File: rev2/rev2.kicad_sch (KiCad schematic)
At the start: 118 parts, among them J1 USB_C_Receptacle_USB2.0_14P, Q1 BSS138, Q10 BSS138, Q11 BSS138, Q12 BSS138, Q13 BSS138, Q14 BSS138, Q15 BSS138, Q16 BSS138, Q2 BSS138, Q3 BSS138, Q4 BSS138, Q5 BSS138, Q6 BSS138, Q7 BSS138, Q8 BSS138, Q9 BSS138, SW1 SW_Push, SW2 SW_Push, SW3 SW_Push, SW4 SW_Push, SW5 SW_Push, SW6 SW_Push, SW7 SW_Push, SW8 SW_Push, U1 CH340N, U2 ATtiny1604-SS, U3 74HC595, U4 74HC595, U5 74HC595, U6 74HC595

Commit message: aw がんばった
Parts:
- renumbered C3 to C2, C2 to C3
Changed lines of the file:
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@@
 		(dnp no)
 		(fields_autoplaced yes)
-		(property "Reference" "C3"
+		(property "Reference" "C2"
 			(at 41.91 220.9799 0)
 			(effects
@@
 			(project "rev2"
 				(path "/039f1884-90f4-4622-bdee-f4fe3d449ea3"
-					(reference "C3")
+					(reference "C2")
 					(unit 1)
 				)
@@
 		(dnp no)
 		(fields_autoplaced yes)
-		(property "Reference" "C2"
+		(property "Reference" "C3"
 			(at 54.61 220.9799 0)
 			(effects
@@
 			(project "rev2"
 				(path "/039f1884-90f4-4622-bdee-f4fe3d449ea3"
-					(reference "C2")
+					(reference "C3")
 					(unit 1)
 				)

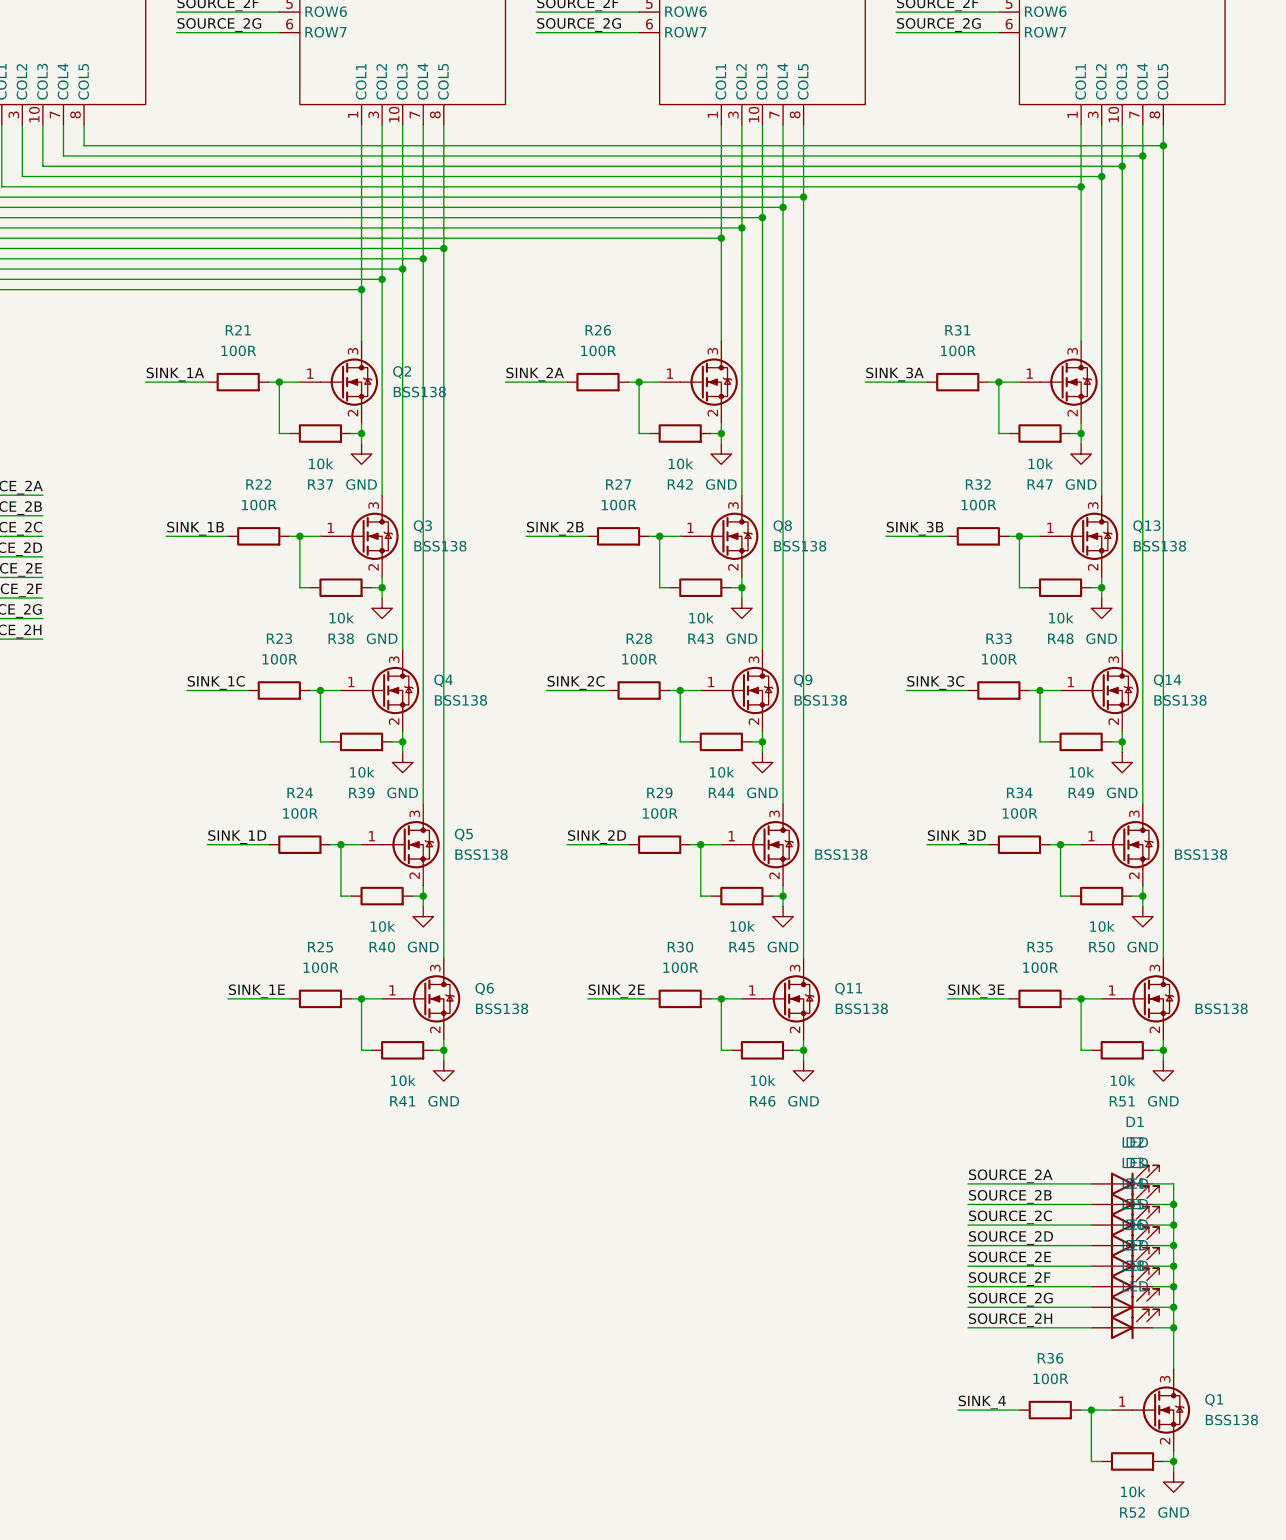
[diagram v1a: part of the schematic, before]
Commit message: 表示器セグメントのシンク回路を単純化した
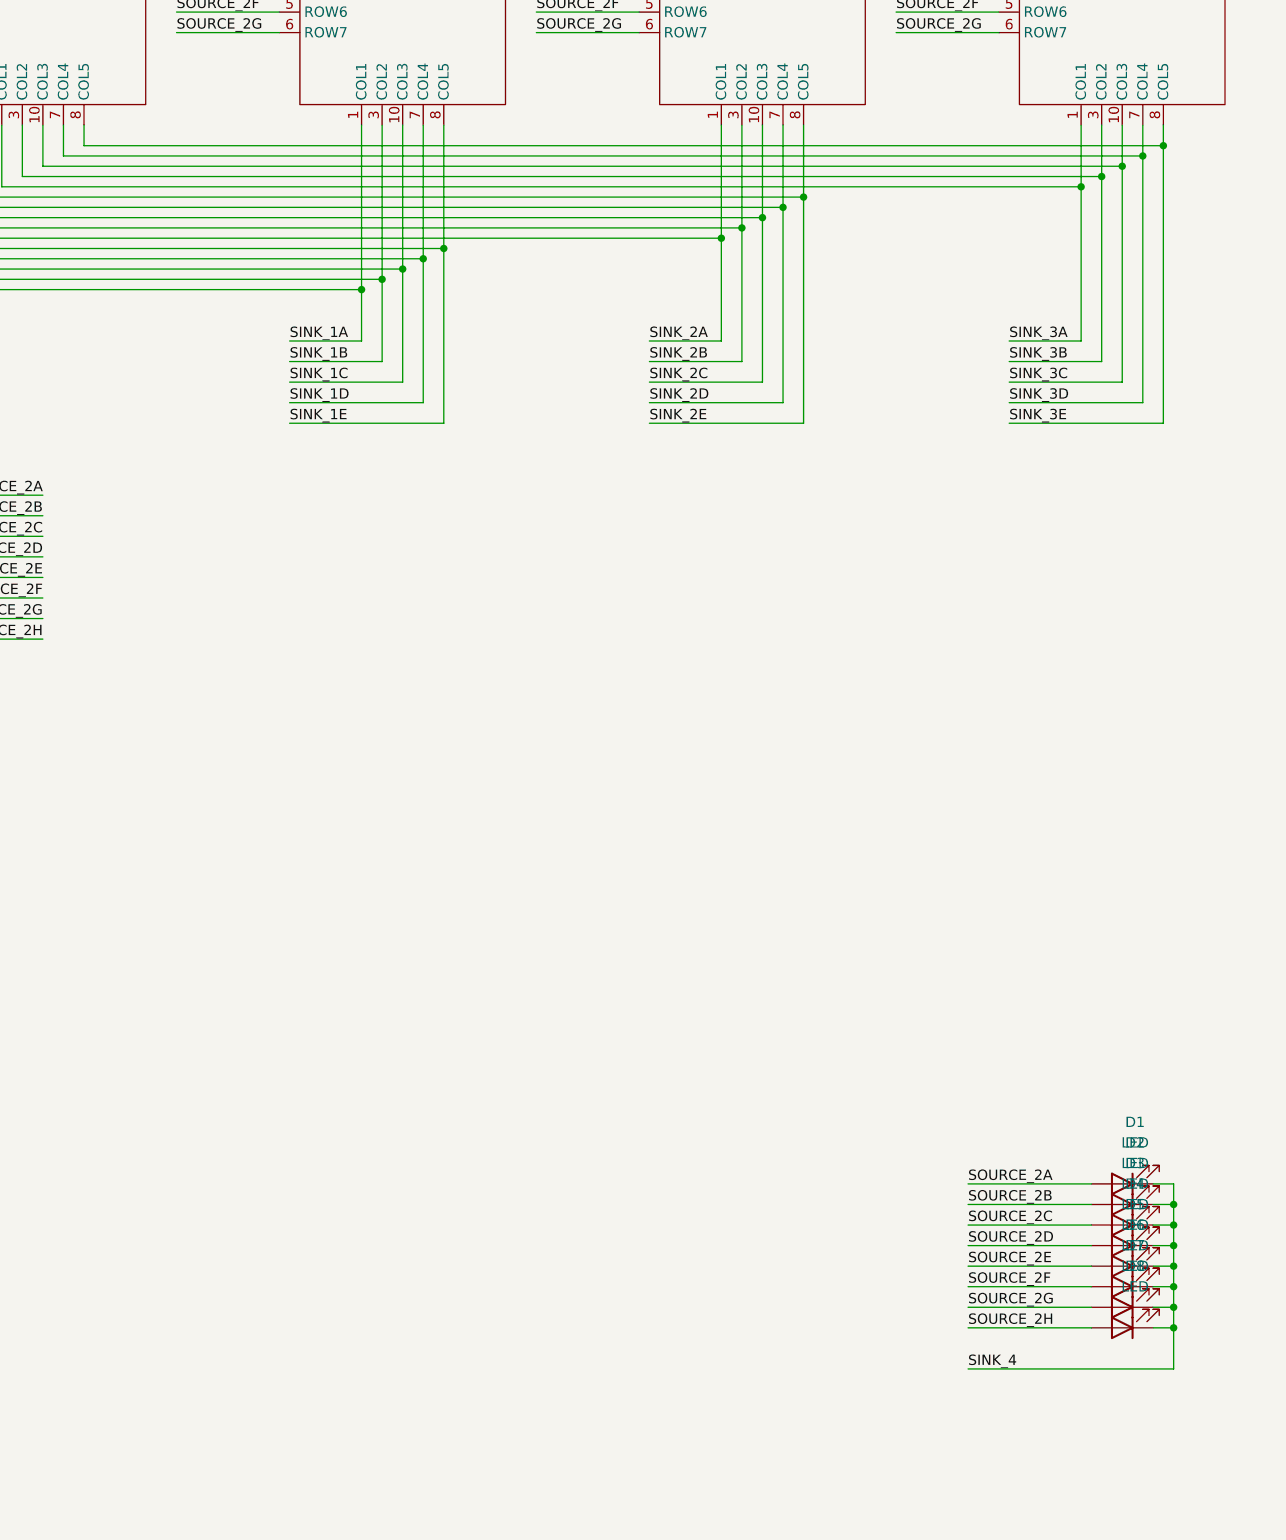
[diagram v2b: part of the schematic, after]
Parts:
- removed Q1, Q10, Q11, Q12, Q13, Q14, Q15, Q16, Q2, Q3, Q4, Q5, Q6, Q7, Q8, Q9: BSS138, Package_TO_SOT_SMD:SOT-23, symbol Transistor_FET:BSS138
- removed R21, R22, R23, R24, R25, R26, R27, R28, R29, R30, R31, R32, R33, R34, R35, R36: 100R, Resistor_SMD:R_0603_1608Metric, symbol Device:R
- removed R37, R38, R39, R40, R41, R42, R43, R44, R45, R46, R47, R48, R49, R50, R51, R52: 10k, Resistor_SMD:R_0603_1608Metric, symbol Device:R
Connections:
- net SINK_1A: now also U10.1 (COL1), U7.1 (COL1)
- net SINK_1B: now also U10.3 (COL2), U7.3 (COL2)
- net SINK_1C: now also U10.10 (COL3), U7.10 (COL3)
- net SINK_1D: now also U10.7 (COL4), U7.7 (COL4)
- net SINK_1E: now also U10.8 (COL5), U7.8 (COL5)
- net SINK_2A: now also U11.1 (COL1), U8.1 (COL1)
- net SINK_2B: now also U11.3 (COL2), U8.3 (COL2)
- net SINK_2C: now also U11.10 (COL3), U8.10 (COL3)
- net SINK_2D: now also U11.7 (COL4), U8.7 (COL4)
- net SINK_2E: now also U11.8 (COL5), U8.8 (COL5)
- net SINK_3A: now also U12.1 (COL1), U9.1 (COL1)
- net SINK_3B: now also U12.3 (COL2), U9.3 (COL2)
- net SINK_3C: now also U12.10 (COL3), U9.10 (COL3)
- net SINK_3D: now also U12.7 (COL4), U9.7 (COL4)
- net SINK_3E: now also U12.8 (COL5), U9.8 (COL5)
- net SINK_4: now also D1.1 (K), D2.1 (K), D3.1 (K), D4.1 (K), D5.1 (K), D6.1 (K), D7.1 (K), D8.1 (K)

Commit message: add connection
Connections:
- net HC595_CLEAR: now also U2.12 (PA2)
- net HC595_CLOCK: now also U2.11 (PA1)
- net HC595_DIN: now also U2.13 (PA3)
- net HC595_EN: now also U2.8 (PB1)
- net HC595_LATCH: now also U2.9 (PB0)
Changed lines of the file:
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@@
+	(wire
+		(pts
+			(xy 93.98 100.33) (xy 78.74 100.33)
+		)
+		(stroke
+			(width 0)
+			(type default)
+		)
+	)
 	(wire
 		(pts
@@
 	(wire
 		(pts
+			(xy 33.02 97.79) (xy 48.26 97.79)
+		)
+		(stroke
+			(width 0)
+			(type default)
+		)
+	)
+	(wire
+		(pts
 			(xy 212.09 63.5) (xy 212.09 73.66)
 		)
@@
 	(wire
 		(pts
+			(xy 33.02 100.33) (xy 48.26 100.33)
+		)
+		(stroke
+			(width 0)
+			(type default)
+		)
+	)
+	(wire
+		(pts
 			(xy 50.8 45.72) (xy 53.34 45.72)
 		)
@@
 	(wire
 		(pts
+			(xy 93.98 102.87) (xy 78.74 102.87)
+		)
+		(stroke
+			(width 0)
+			(type default)
+		)
+	)
+	(wire
+		(pts
 			(xy 295.91 82.55) (xy 295.91 92.71)
 		)
@@
 		(pts
 			(xy 231.14 111.76) (xy 226.06 111.76)
+		)
+		(stroke
+			(width 0)
+			(type default)
+		)
+	)
+	(wire
+		(pts
+			(xy 93.98 105.41) (xy 78.74 105.41)
 		)
 		(stroke
@@
 		)
 	)
+	(label "HC595_EN"
+		(at 33.02 100.33 0)
+		(effects
+			(font
+				(size 1.27 1.27)
+			)
+			(justify left bottom)
+		)
+	)
 	(label "SINK_1A"
 		(at 284.48 90.17 0)
@@
 		)
 	)
+	(label "HC595_DIN"
+		(at 93.98 105.41 180)
+		(effects
+			(font
+				(size 1.27 1.27)
+			)
+			(justify right bottom)
+		)
+	)
 	(label "READ_1"
 		(at 133.35 72.39 180)
@@
 		)
 	)
+	(label "HC595_CLEAR"
+		(at 93.98 102.87 180)
+		(effects
+			(font
+				(size 1.27 1.27)
+			)
+			(justify right bottom)
+		)
+	)
 	(label "SINK_1D"
 		(at 165.1 167.64 180)
@@
 		)
 	)
+	(label "HC595_LATCH"
+		(at 33.02 97.79 0)
+		(effects
+			(font
+				(size 1.27 1.27)
+			)
+			(justify left bottom)
+		)
+	)
 	(label "SINK_1A"
 		(at 165.1 160.02 180)
@@
 		)
 	)
+	(label "HC595_CLOCK"
+		(at 93.98 100.33 180)
+		(effects
+			(font
+				(size 1.27 1.27)
+			)
+			(justify right bottom)
+		)
+	)
